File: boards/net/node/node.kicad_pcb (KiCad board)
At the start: 2 copper layers, 50 x 50 mm, 0 parts

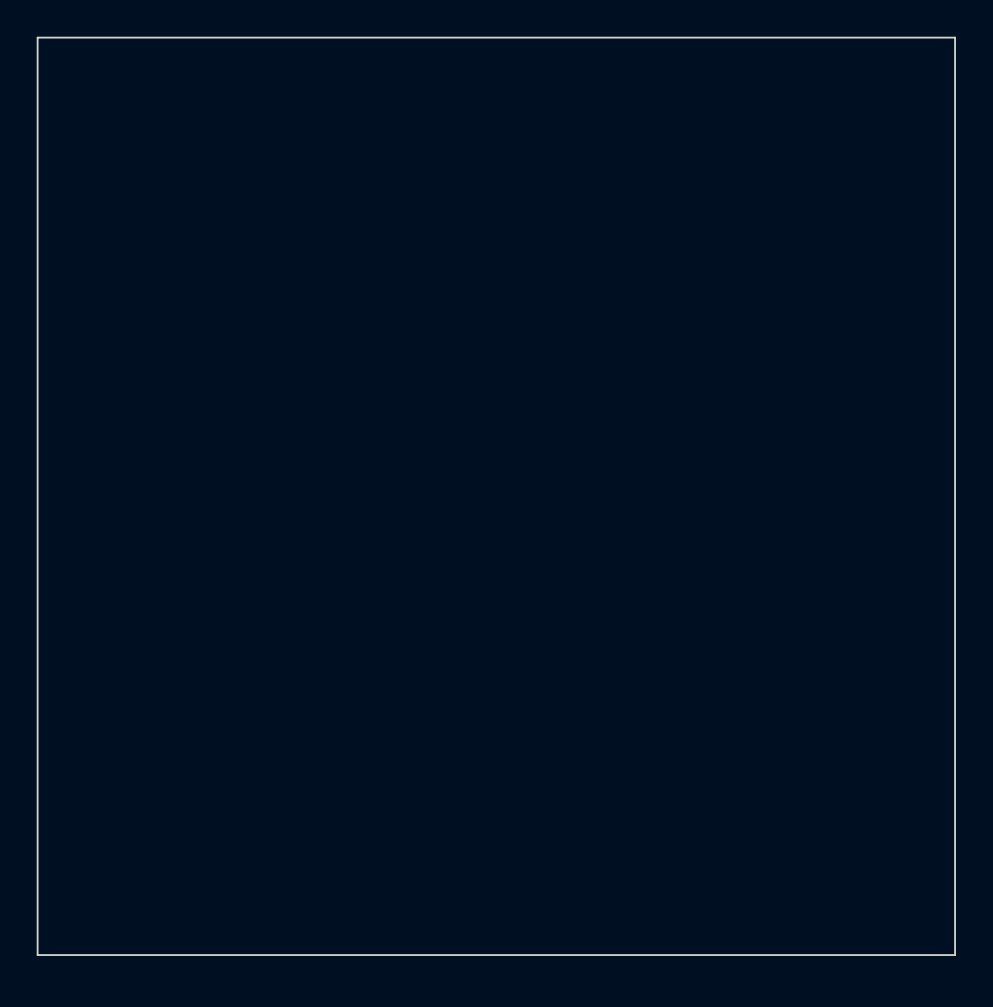
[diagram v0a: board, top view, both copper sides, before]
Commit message: net/node: PCB placement (48 x 48, 4 layers); pcbgen: copper_layers, repo footprint lib, dnp/exclude attrs
Placement only; no routing yet. RP2040 rot 180 top-left with the flash below and
crystal above, LEDs centred, buzzer right, pogo pads bottom-left, sensor and header
along the bottom. Inner layers: GND (In1) and 3V3 (In2) planes.

Co-Authored-By: Claude Fable 5.1 <noreply@anthropic.com>
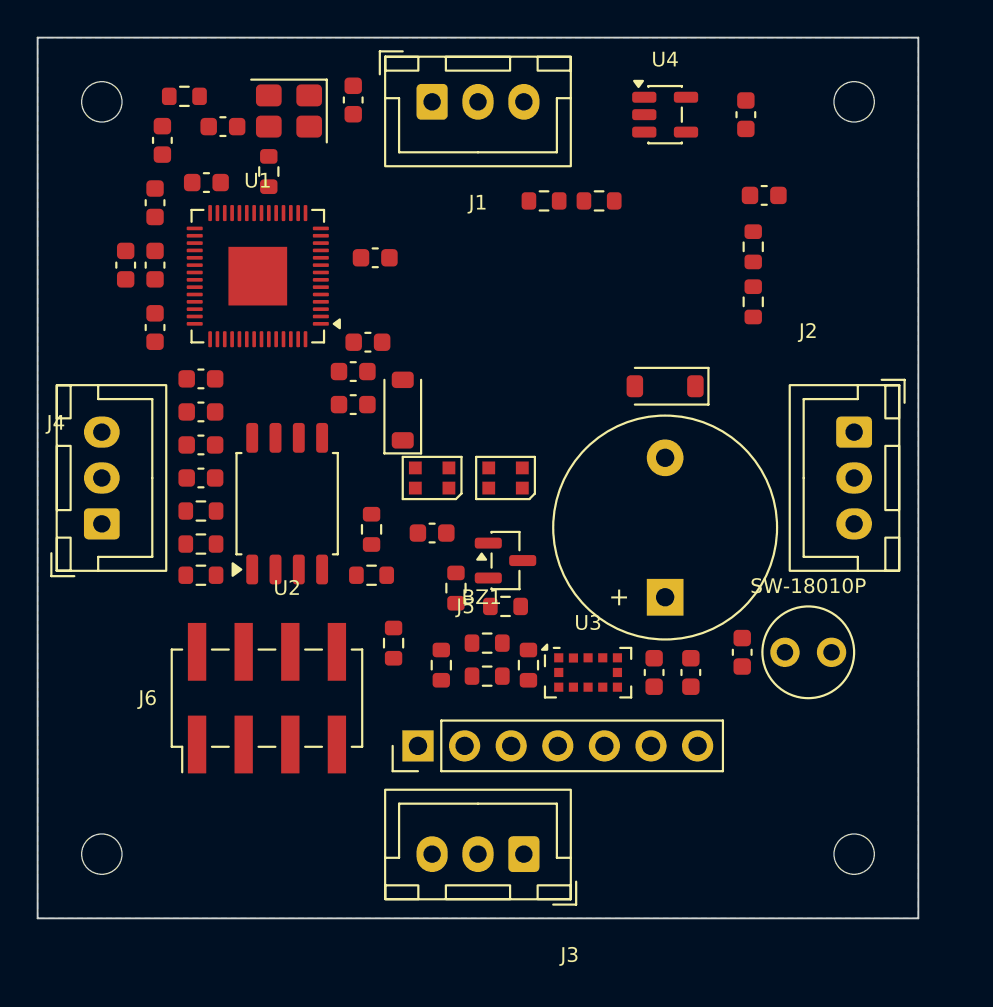
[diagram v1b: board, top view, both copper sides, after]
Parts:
- added BZ1: Buzzer 5V, Buzzer_Beeper:Buzzer_12x9.5RM7.6, F.Cu at (84.2, 80.5)
- added C1: 27p, Capacitor_SMD:C_0603_1608Metric, F.Cu at (67.2, 53.4)
- added C10: 100n, Capacitor_SMD:C_0603_1608Metric, F.Cu at (56.4, 59.0)
- added C11: 1u, Capacitor_SMD:C_0603_1608Metric, F.Cu at (58.9, 70.4)
- added C12: 10u, Capacitor_SMD:C_0603_1608Metric, F.Cu at (54.8, 62.4)
- added C13: 1u, Capacitor_SMD:C_0603_1608Metric, F.Cu at (67.2, 68.2)
- added C14: 100n, Capacitor_SMD:C_0603_1608Metric, F.Cu at (56.8, 55.6)
- added C15: 100n, Capacitor_SMD:C_0603_1608Metric, F.Cu at (58.9, 72.2)
- added C16: 100n, Capacitor_SMD:C_0603_1608Metric, F.Cu at (58.9, 74.0)
- added C17: 10u, Capacitor_SMD:C_0603_1608Metric, F.Cu at (88.6, 54.2)
- added C18: 10u, Capacitor_SMD:C_0603_1608Metric, F.Cu at (89.6, 58.6)
- added C19: 100n, Capacitor_SMD:C_0603_1608Metric, F.Cu at (71.5, 77.0)
- added C2: 27p, Capacitor_SMD:C_0603_1608Metric, F.Cu at (60.1, 54.9)
- added C20: 100n, Capacitor_SMD:C_0603_1608Metric, F.Cu at (83.6, 84.6)
- added C21: 4u7, Capacitor_SMD:C_0603_1608Metric, F.Cu at (85.6, 84.6)
- added C22: 100n, Capacitor_SMD:C_0603_1608Metric, F.Cu at (88.4, 83.5)
- added C3: 100n, Capacitor_SMD:C_0603_1608Metric, F.Cu at (68.0, 66.6)
- added C4: 100n, Capacitor_SMD:C_0603_1608Metric, F.Cu at (68.4, 62.0)
- added C5: 100n, Capacitor_SMD:C_0603_1608Metric, F.Cu at (59.2, 57.9)
- added C6: 100n, Capacitor_SMD:C_0603_1608Metric, F.Cu at (56.4, 62.4)
- added C7: 100n, Capacitor_SMD:C_0603_1608Metric, F.Cu at (56.4, 65.8)
- added C8: 100n, Capacitor_SMD:C_0603_1608Metric, F.Cu at (58.9, 68.6)
- added C9: 100n, Capacitor_SMD:C_0603_1608Metric, F.Cu at (67.2, 70.0)
- added D1: 1N4148W, Diode_SMD:D_SOD-123, F.Cu at (69.9, 70.3)
- added D2: WS2812B-2020, LED_SMD:LED_WS2812B-2020_PLCC4_2.0x2.0mm, F.Cu at (71.5, 74.0)
- added D3: 1N4148W, Diode_SMD:D_SOD-123, F.Cu at (84.2, 69.0)
- added D4: WS2812B-2020, LED_SMD:LED_WS2812B-2020_PLCC4_2.0x2.0mm, F.Cu at (75.5, 74.0)
- added H1: M2, MountingHole:MountingHole_2.2mm_M2, F.Cu at (53.5, 53.5)
- added H2: M2, MountingHole:MountingHole_2.2mm_M2, F.Cu at (94.5, 53.5)
- added H3: M2, MountingHole:MountingHole_2.2mm_M2, F.Cu at (53.5, 94.5)
- added H4: M2, MountingHole:MountingHole_2.2mm_M2, F.Cu at (94.5, 94.5)
- added J1: N, Connector_JST:JST_XH_B3B-XH-A_1x03_P2.50mm_Vertical, F.Cu at (71.5, 53.5)
- added J2: E, Connector_JST:JST_XH_B3B-XH-A_1x03_P2.50mm_Vertical, F.Cu at (94.5, 71.5)
- added J3: S, Connector_JST:JST_XH_B3B-XH-A_1x03_P2.50mm_Vertical, F.Cu at (76.5, 94.5)
- added J4: W, Connector_JST:JST_XH_B3B-XH-A_1x03_P2.50mm_Vertical, F.Cu at (53.5, 76.5)
- added J5: SENSOR, Connector_PinHeader_2.54mm:PinHeader_1x07_P2.54mm_Vertical, F.Cu at (70.7, 88.6)
- added J6: PROG, Connector_PinHeader_2.54mm:PinHeader_2x04_P2.54mm_Vertical_SMD, F.Cu at (62.5, 86.0)
- added Q1: 2N7002, Package_TO_SOT_SMD:SOT-23, F.Cu at (75.5, 78.5)
- added R1: 1k, Resistor_SMD:R_0603_1608Metric, F.Cu at (62.6, 57.3)
- added R10: 4k7, Resistor_SMD:R_0603_1608Metric, F.Cu at (89.0, 61.4)
- added R11: 100, Resistor_SMD:R_0603_1608Metric, F.Cu at (72.0, 84.2)
- added R12: 4k7, Resistor_SMD:R_0603_1608Metric, F.Cu at (69.4, 83.0)
- added R13: 100, Resistor_SMD:R_0603_1608Metric, F.Cu at (58.9, 77.6)
- added R14: 4k7, Resistor_SMD:R_0603_1608Metric, F.Cu at (58.9, 75.8)
- added R15: 27, Resistor_SMD:R_0603_1608Metric, F.Cu at (58.9, 79.3)
- added R16: 27, Resistor_SMD:R_0603_1608Metric, F.Cu at (68.2, 79.3)
- added R17: 1k, Resistor_SMD:R_0603_1608Metric, F.Cu at (72.8, 80.0)
- added R18: 100k, Resistor_SMD:R_0603_1608Metric, F.Cu at (75.5, 81.0)
- added R2: 10k, Resistor_SMD:R_0603_1608Metric, F.Cu at (58.0, 53.2)
- added R3: 10k, Resistor_SMD:R_0603_1608Metric, F.Cu at (68.2, 76.8)
- added R4: 4k7, Resistor_SMD:R_0603_1608Metric, F.Cu at (74.5, 84.8)
- added R5: 4k7, Resistor_SMD:R_0603_1608Metric, F.Cu at (76.8, 84.2)
- added R6: 10k, Resistor_SMD:R_0603_1608Metric, F.Cu at (74.5, 83.0)
- added R7: 100, Resistor_SMD:R_0603_1608Metric, F.Cu at (77.6, 58.9)
- added R8: 4k7, Resistor_SMD:R_0603_1608Metric, F.Cu at (80.6, 58.9)
- added R9: 100, Resistor_SMD:R_0603_1608Metric, F.Cu at (89.0, 64.4)
- added SW1: SW-18010P, boards:SW-18010P, F.Cu at (92.0, 83.5)
- added U1: RP2040, Package_DFN_QFN:QFN-56-1EP_7x7mm_P0.4mm_EP3.2x3.2mm, F.Cu at (62.0, 63.0)
- added U2: W25Q16JVSSIQ, Package_SO:SOIC-8_5.3x5.3mm_P1.27mm, F.Cu at (63.6, 75.4)
- added U3: VL53L0CXV0DH/1, OptoDevice:ST_VL53L0X, F.Cu at (80.0, 84.6)
- added U4: ME6211C33M5G, Package_TO_SOT_SMD:SOT-23-5, F.Cu at (84.2, 54.2)
- added Y1: 12MHz, Crystal:Crystal_SMD_3225-4Pin_3.2x2.5mm, F.Cu at (63.7, 54.0)
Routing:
- added copper zone on In2.Cu, net +3V3
- added copper zone on B.Cu, net GND
- added copper zone on In1.Cu, net GND
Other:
- board size 50 x 50 mm -> 48 x 48 mm
- copper layers 2 -> 4

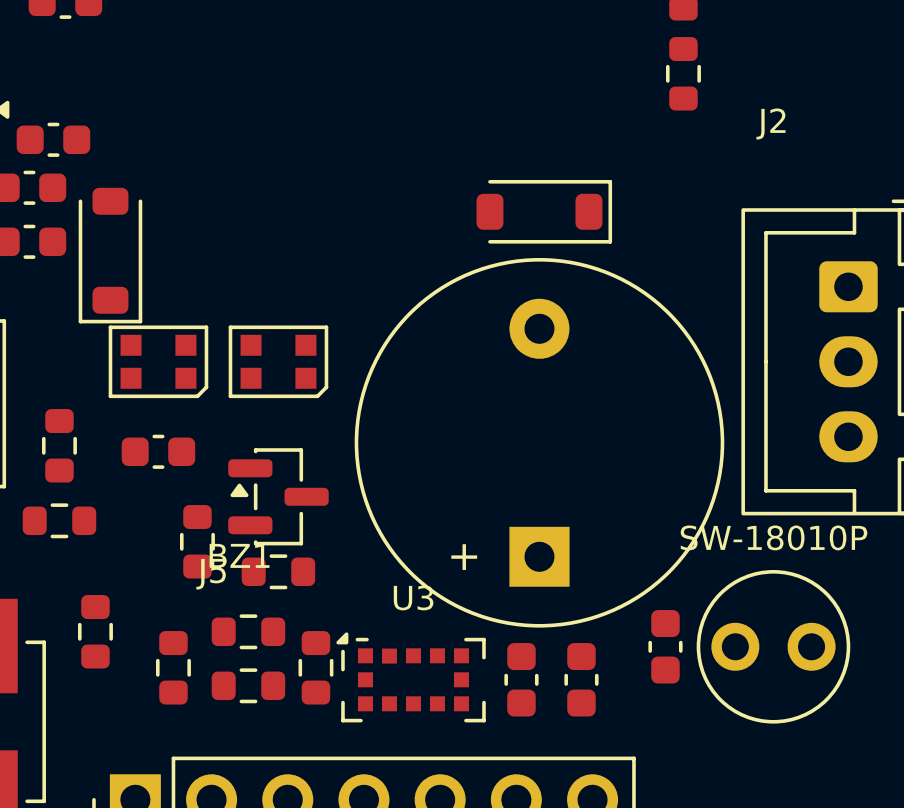
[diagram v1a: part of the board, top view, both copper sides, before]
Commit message: net/node: drop the buzzer; pcbgen: idempotent inner layers, attr-less footprints keep flags, board-side variants
- pcbgen: InN.Cu layers are rebuilt from scratch (a generator reading its own output
  no longer accumulates copies); footprints without an attr clause still get dnp /
  exclude flags; per-variant dnp/exclude overrides from the netlist are written as
  KiCad 10 (variants ...) on the board and (variant ...) on each footprint, so
  `pcb export pos --variant` now agrees with the BOM. Tests cover all three.
- net/node: BZ1/Q1/R17/R18/D3 removed (largest part after the connectors, and a 5 V
  budget problem next to the LEDs); GPIO5 is a no-connect. ERC clean. README: buzzer
  decision, jig row spacing (5.05 mm), D4 two-pixel note, LCSC list.

Co-Authored-By: Claude Fable 5.1 <noreply@anthropic.com>
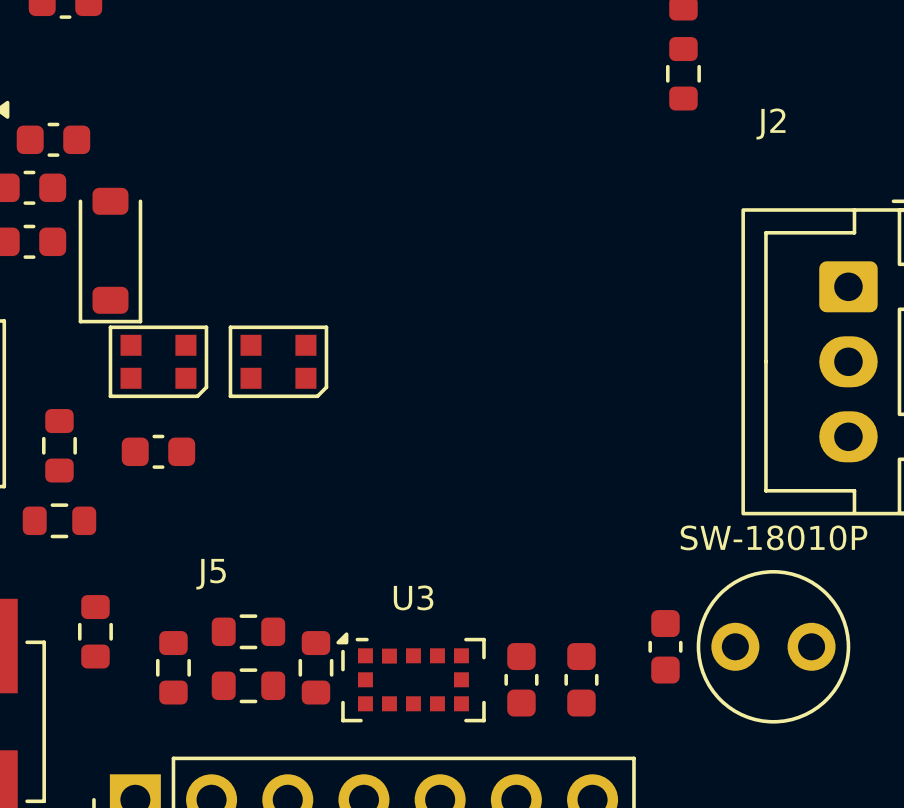
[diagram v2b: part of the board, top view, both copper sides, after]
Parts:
- removed BZ1: Buzzer 5V, Buzzer_Beeper:Buzzer_12x9.5RM7.6
- removed D3: 1N4148W, Diode_SMD:D_SOD-123
- removed Q1: 2N7002, Package_TO_SOT_SMD:SOT-23
- removed R17: 1k, Resistor_SMD:R_0603_1608Metric
- removed R18: 100k, Resistor_SMD:R_0603_1608Metric
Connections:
- U1 pad 7: /BUZZ -> unconnected-(U1-GPIO5-Pad7)

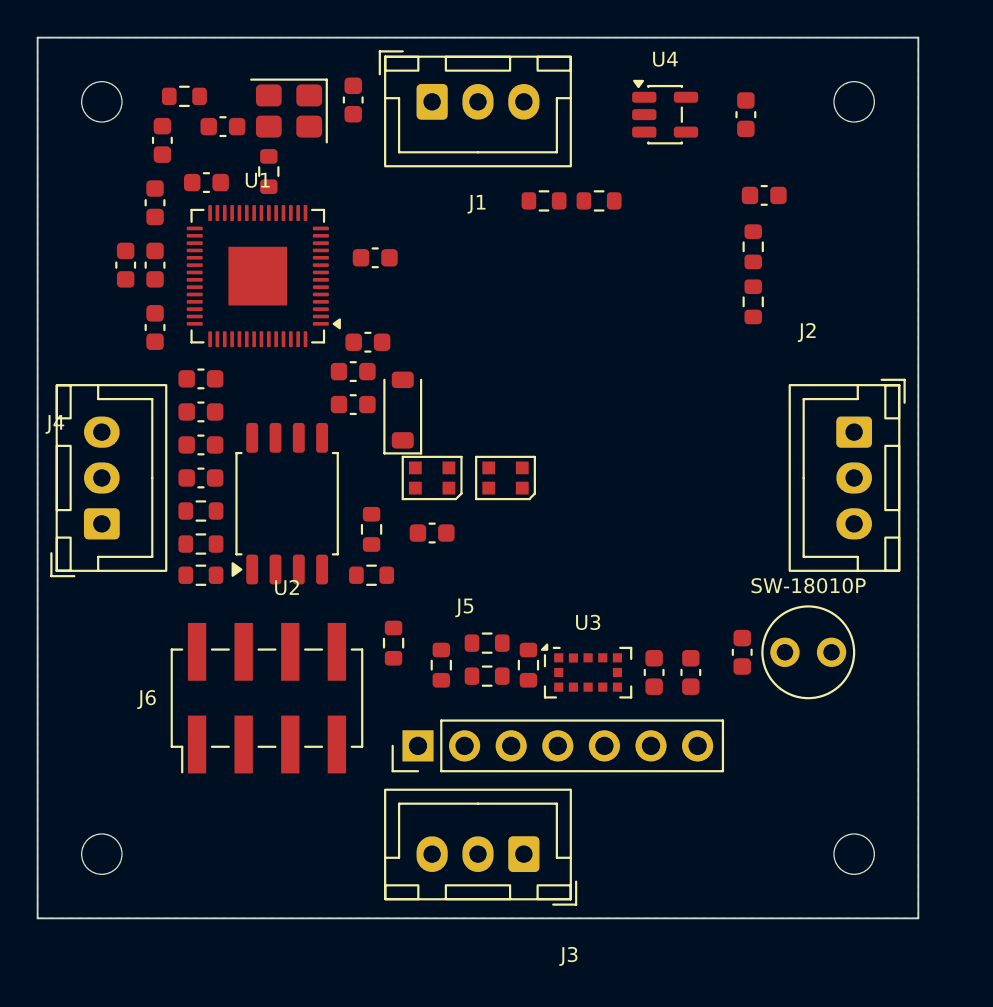
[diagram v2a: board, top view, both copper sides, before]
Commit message: net/node: place and route the board (DRC clean); pcbgen: solid_pads, zone thermals, empty fields
- Sensor GPIOs moved: XSHUT GPIO7->GPIO5, SDA/SCL GPIO8/9 -> GPIO10/11 (I2C1) so IOVDD
  pin 10's neighbours stay unrouted and it can via to the plane; J6 USB pins swapped
  (1 = DM, 3 = DP) so the traces do not cross. Schematic regenerated, ERC clean.
- pcb.py: U1 at (14, 13), 4 layers, every net routed: up-left SWD/crystal fan onto
  1.2 mm rows, down-right GPIO fan onto 0.7 mm columns, QSPI around the flash, west
  B.Cu lanes ending in vias inside the pogo pads, 0.8 mm 5 V ring notched around three
  M2 keepouts and open at the top-left corner, planes on In1/In2. make check: 0
  violations, 0 unconnected, 0 parity issues (two dangling-end warnings = the open ring).
- pcbgen: solid_pads= (J4 pin 3), zone thermal_gap/thermal_bridge, empty schematic fields
  written as empty properties (parity), ref_pos documented as rotating with the part.
- READMEs: PCB section rewritten for the routed board, resume path, generate commands.
  CLAUDE.md: 0.4 mm pitch escape/via rules, pad offsets, flatpak KiCad setup.

Co-Authored-By: Claude Fable 5.1 <noreply@anthropic.com>
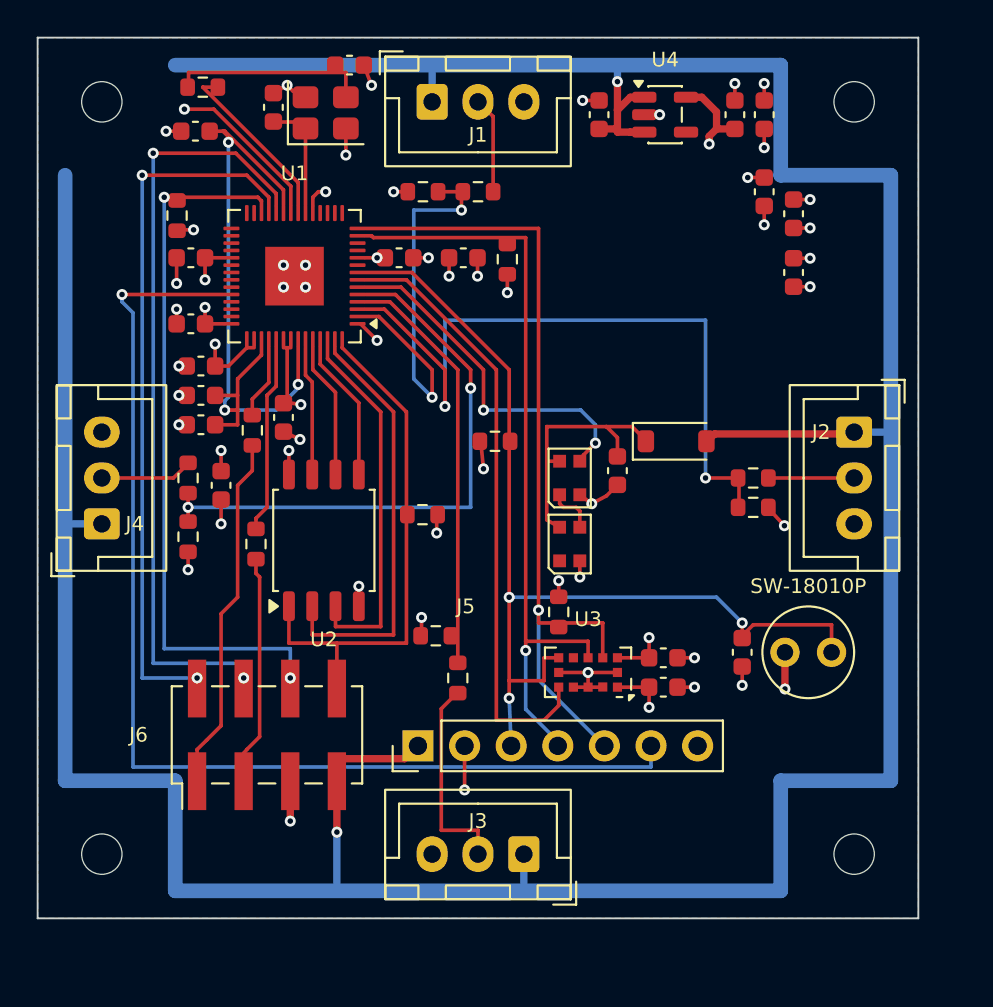
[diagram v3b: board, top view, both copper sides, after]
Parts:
- moved C12 35.8 mm to (89.6, 54.2)
- moved C11 33.2 mm to (91.2, 62.8), turned to 90 degrees
- moved C8 32.4 mm to (89.6, 58.4), turned to 90 degrees
- moved C5 32.0 mm to (91.2, 59.6), turned to 90 degrees
- moved R4 22.8 mm to (75.6, 62.1), turned to 90 degrees
- moved D1 15.0 mm to (84.8, 72.0), turned to 0 degrees
- moved R10 14.2 mm to (89.0, 75.6), turned to 180 degrees
- moved R6 11.0 mm to (74.9, 72.0)
- moved C19 10.7 mm to (81.6, 73.6), turned to -90 degrees
- moved R8 9.61 mm to (71.0, 58.4), turned to 0 degrees
- moved R9 9.60 mm to (89.0, 74.0), turned to 0 degrees
- moved C10 9.24 mm to (58.9, 67.9), turned to 180 degrees
- moved C13 8.40 mm to (58.9, 69.5), turned to 180 degrees
- moved R15 8.38 mm to (61.7, 71.4), turned to 90 degrees
- moved C17 8.00 mm to (80.6, 54.2)
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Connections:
- R15 pad 2: /USB_DP -> /USB_DM
- R16 pad 2: /USB_DM -> /USB_DP
- U1 pad 11: /SDA -> unconnected-(U1-GPIO8-Pad11)
- U1 pad 12: /SCL -> unconnected-(U1-GPIO9-Pad12)
- U1 pad 13: unconnected-(U1-GPIO10-Pad13) -> /SDA
- U1 pad 14: unconnected-(U1-GPIO11-Pad14) -> /SCL
- U1 pad 7: unconnected-(U1-GPIO5-Pad7) -> /SENS_XSHUT
- U1 pad 9: /SENS_XSHUT -> unconnected-(U1-GPIO7-Pad9)
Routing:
- net +5V: track 0.00 -> 202.0 mm, vias 0 -> 2
- net /SENS_AIN: track 0.00 -> 60.9 mm, vias 0 -> 1
- net /SENS_INT: track 0.00 -> 55.2 mm, vias 0 -> 3
- net +3V3: track 0.00 -> 51.4 mm, vias 0 -> 27
- net /SCL: track 0.00 -> 45.2 mm, vias 0 -> 1
- net /SWCLK: track 0.00 -> 41.8 mm, vias 0 -> 2
- net /SDA: track 0.00 -> 41.5 mm, vias 0 -> 1
- net /RUN: track 0.00 -> 38.7 mm, vias 0 -> 2
- net /LINK_E: track 0.00 -> 38.6 mm, vias 0 -> 2
- net /SWDIO: track 0.00 -> 38.2 mm, vias 0 -> 2
- net GND: track 0.00 -> 37.7 mm, vias 0 -> 34
- net /DVDD: track 0.00 -> 35.3 mm, vias 0 -> 3
- net /SENS_XSHUT: track 0.00 -> 33.0 mm
- net /LINK_W: track 0.00 -> 32.0 mm, vias 0 -> 2
- net /QSPI_SS: track 0.00 -> 28.5 mm
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
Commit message: net/node: place and route the piezo (BZ1 right of U1, R17/R18 by U4, GPIO12/13 on rows y 7.0/6.2)
make check: 0 violations, 0 unconnected, 0 parity issues (open-ring warnings only).
R7's J1 leg moved to B.Cu under the two new rows.

Co-Authored-By: Claude Fable 5.1 <noreply@anthropic.com>
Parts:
- added BZ1: PKMCS0909E4000-R1, Buzzer_Beeper:Buzzer_Murata_PKMCS0909E, F.Cu at (84.0, 64.4)
- added R17: 100, Resistor_SMD:R_0603_1608Metric, F.Cu at (81.0, 58.3)
- added R18: 100, Resistor_SMD:R_0603_1608Metric, F.Cu at (81.0, 56.7)
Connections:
- U1 pad 15: unconnected-(U1-GPIO12-Pad15) -> /BUZZ_A
- U1 pad 16: unconnected-(U1-GPIO13-Pad16) -> /BUZZ_B
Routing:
- net Net-(BZ1-+): track 0.00 -> 17.0 mm
- net /BUZZ_B: track 0.00 -> 15.5 mm
- net /BUZZ_A: track 0.00 -> 15.0 mm
- net Net-(BZ1--): track 0.00 -> 4.43 mm
- net Net-(J1-Pin_2): track 5.25 -> 7.25 mm, vias 0 -> 1
